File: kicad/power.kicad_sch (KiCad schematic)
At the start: 54 parts, among them J1 L, J2 N, J3 PE, J4 PE, J5 VOUT+, J6 VOUT-, Q5 BD677, U2 AP64060QWU, U3 AP64060QWU

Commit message: Commit
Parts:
- added F2: 0PTF0078P, footprints:FuseHolder, symbol Device:Fuse
- added J12: VCC, TestPoint:TestPoint_Pad_4.0x4.0mm, symbol Connector_Generic:Conn_01x01
- added J9: GND, TestPoint:TestPoint_Pad_4.0x4.0mm, symbol Connector_Generic:Conn_01x01
- C13, C21: MPN CL21B105KBFNNNF -> CL21B105KBFNNNF
- C22, C56: MPN CL31A106KBHNNNE -> CL31A106KBHNNNE
- JP1, TP6: now left out of the parts list
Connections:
- net GND: now also J9.1 (Pin_1)
- net VDD: now also F2.1; no longer C15.1, JP1.2 (B), Q5.3 (E), TP6.1
- net VCC: now reaches C16.1, C17.1, D7.1 (+), JP1.1 (A), Q5.2 (C), R27.2, R29.1
- net VCC: now also J12.1 (Pin_1)
- new net: C15.1, F2.2, JP1.2 (B), Q5.3 (E), TP6.1
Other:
- moved on the sheet: C15, C16, C17, C18, D7, HS3, JP1, Q5, R27, R28, R29, R30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

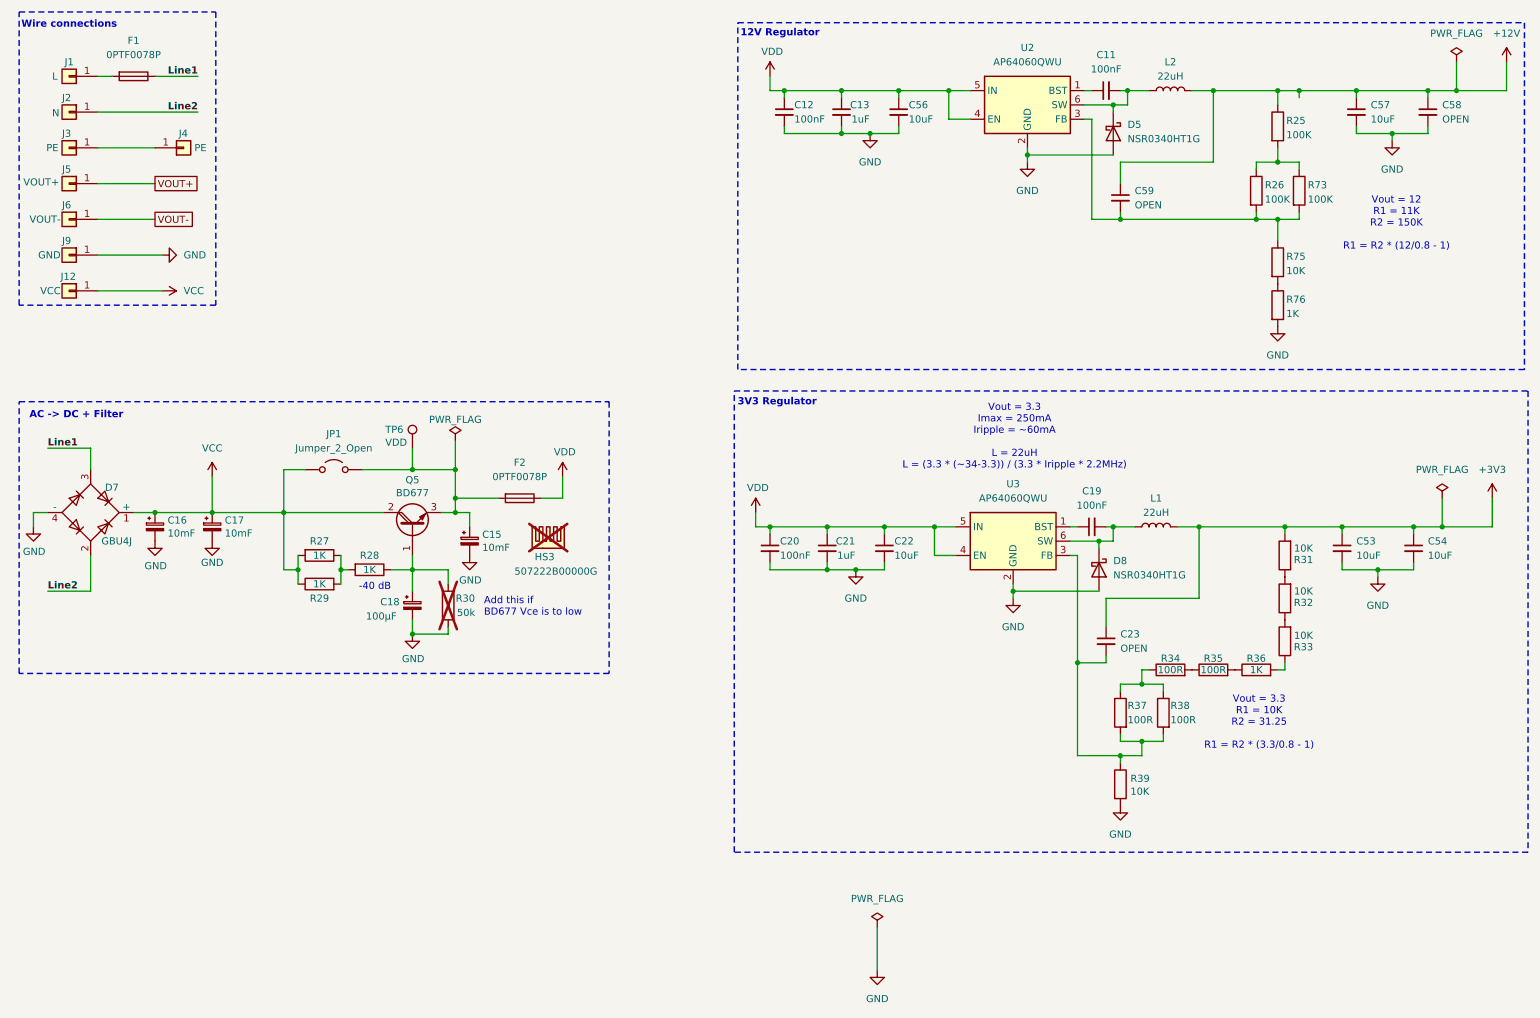
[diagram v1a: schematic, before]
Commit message: Added more caps on SMPS outputs
- Added pin header for BOOT and RST
- Re added USBLC6-2SC6
  - can be connected to VBUS or 3V3
- 0R option to connect usb shield to GND
- Added solder pad for 12V
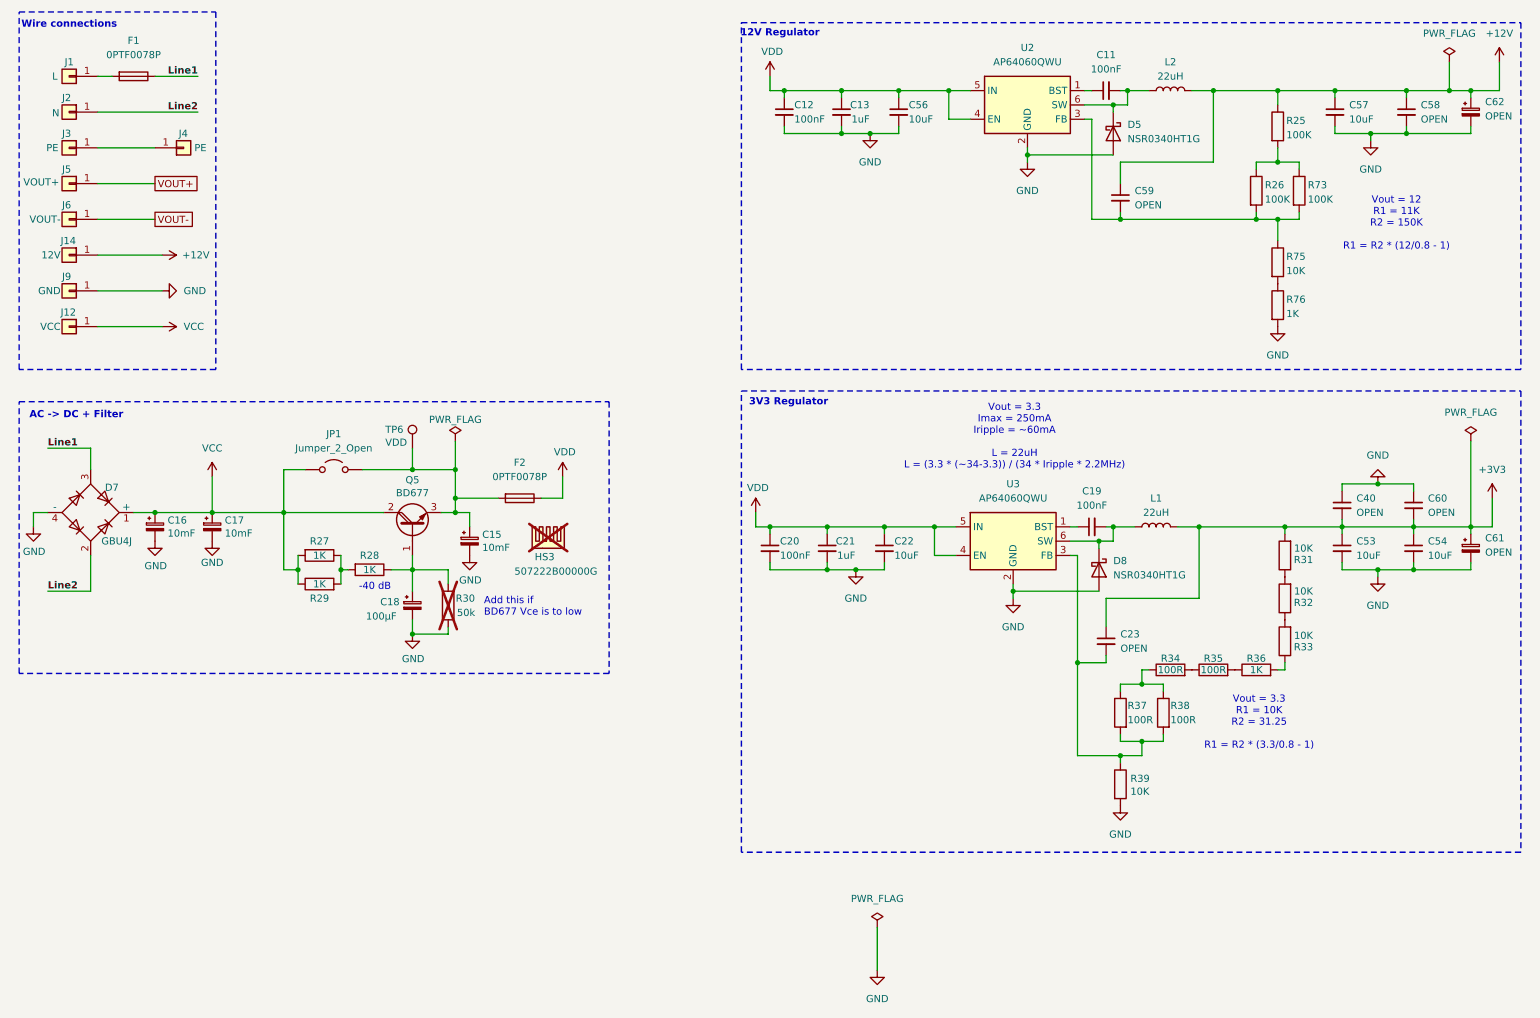
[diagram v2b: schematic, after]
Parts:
- added C40, C60: OPEN, Capacitor_SMD:C_0805_2012Metric_Pad1.18x1.45mm_HandSolder, symbol Device:C_Small
- added C61, C62: OPEN, Capacitor_THT:CP_Radial_D6.3mm_P2.50mm, symbol Device:C_Polarized_Small
- added J14: 12V, TestPoint:TestPoint_Pad_4.0x4.0mm, symbol Connector_Generic:Conn_01x01
- L1: MPN AMRM00101040220MA1 -> AMRM00101040220MA1
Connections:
- net +12V: now also C62.1, J14.1 (Pin_1)
- net +3V3: now also C40.2, C60.2, C61.1
- net GND: now also C40.1, C60.1, C61.2, C62.2
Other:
- note added: "Vout = 3.3 Imax = 250mA Iripple = ~60mA L = 22uH L = (3.3 * (~34-3.3)) / (34 * Iripple * 2.2MHz)"
- note removed: "Vout = 3.3 Imax = 250mA Iripple = ~60mA L = 22uH L = (3.3 * (~34-3.3)) / (3.3 * Iripple * 2.2MHz)"
- moved on the sheet: C57, C58, J12, J9

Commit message: Removed unnecessary caps and other shit
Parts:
- removed C13, C21: 1uF, Capacitor_SMD:C_0805_2012Metric_Pad1.18x1.45mm_HandSolder, symbol Device:C_Small
- removed C17: 10mF, symbol Device:C_Polarized_Small
- removed C40, C58, C60: OPEN, Capacitor_SMD:C_0805_2012Metric_Pad1.18x1.45mm_HandSolder, symbol Device:C_Small
- removed C61: OPEN, Capacitor_THT:CP_Radial_D6.3mm_P2.50mm, symbol Device:C_Polarized_Small
- C27: renamed from C16; footprint (none) -> Capacitor_THT:CP_Radial_D30.0mm_P10.00mm_SnapIn
- C29: renamed from C15; footprint (none) -> Capacitor_THT:CP_Radial_D30.0mm_P10.00mm_SnapIn
- R31: renamed from R27; now not fitted
- renumbered C11 to C17, C12 to C18, C56 to C20, C57 to C21, C62 to C23, C59 to C24, C19 to C28, C20 to C30, C22 to C32, C53 to C33, C54 to C34, C18 to C36, C23 to C37, D7 to D6, D8 to D7, J14 to J7, J9 to J8, J12 to J9, L2 to L1, L1 to L2, R25 to R26, R26 to R27, R73 to R28, R75 to R29, R76 to R30, R31 to R32, R28 to R33, R29 to R34, R32 to R35, R30 to R36, R33 to R37, R34 to R38, R35 to R39, R36 to R40, R37 to R41, R38 to R42, R39 to R43
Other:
- moved on the sheet: C18, C23, C30

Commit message: IDK
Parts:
- renumbered C17 to C12, C18 to C13, C20 to C14, C21 to C15, C23 to C16, C24 to C17, C27 to C18, C28 to C19, C29 to C20, C30 to C21, C32 to C22, C33 to C23, C34 to C24, C36 to C25, C37 to C26

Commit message: Fixed bug in schematic
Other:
- moved on the sheet: F2
